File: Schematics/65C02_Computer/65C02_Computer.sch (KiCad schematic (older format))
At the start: 11 parts

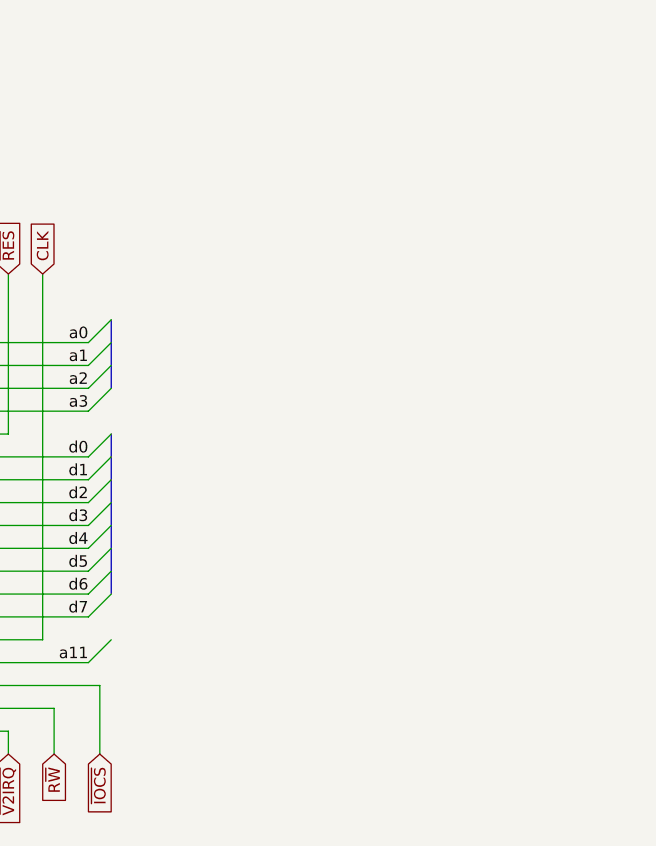
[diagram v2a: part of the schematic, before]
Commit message: Added ACIA chip
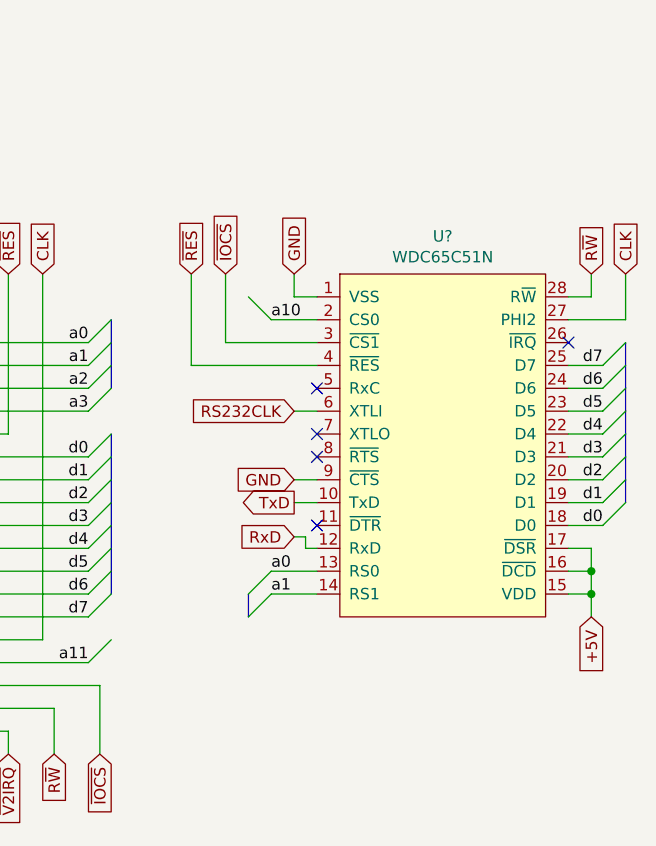
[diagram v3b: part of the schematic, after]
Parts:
- added U?: WDC65C51N, Package_DIP:DIP-28_W15.24mm_Socket, symbol 6502:WDC65C51N
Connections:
- net +5V: now also U?.15 (VDD), U?.16 (~DCD), U?.17 (~DSR)
- net CLK: now also U?.27 (PHI2)
- net GND: now also U?.1 (VSS), U?.9 (~CTS)
- net RS232CLK: now also U?.6 (XTLI)
- net R~W: now also U?.28 (R~W)
- net a0: now also U?.13 (RS0)
- net a1: now also U?.14 (RS1)
- net a10: now also U?.2 (CS0)
- net d0: now also U?.18 (D0)
- net d1: now also U?.19 (D1)
- net d2: now also U?.20 (D2)
- net d3: now also U?.21 (D3)
- net d4: now also U?.22 (D4)
- net d5: now also U?.23 (D5)
- net d6: now also U?.24 (D6)
- net d7: now also U?.25 (D7)
- net ~IOCS: now also U?.3 (~CS1)
- net ~RES: now also U?.4 (~RES)
- new net RxD: U?.12 (RxD)
- new net TxD: U?.10 (TxD)
- no-connect marks 15 -> 20
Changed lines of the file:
@@
 Wire Wire Line
 	5950 4600 5950 4500
+$Comp
+L 6502:WDC65C51N U?
+U 1 1 5E222305
+P 9100 3250
+F 0 "U?" H 9100 4165 50  0000 C CNN
+F 1 "WDC65C51N" H 9100 4074 50  0000 C CNN
+F 2 "Package_DIP:DIP-28_W15.24mm_Socket" H 9100 3250 50  0001 C CNN
+F 3 "https://www.westerndesigncenter.com/wdc/documentation/w65c51n.pdf" H 9100 3250 50  0001 C CNN
+	1    9100 3250
+	1    0    0    -1
+$EndComp
+Text GLabel 9750 4000 3    50   Input ~ 0
++5V
+Wire Wire Line
+	9650 3900 9750 3900
+Wire Wire Line
+	9750 3900 9750 4000
+Text GLabel 8450 2500 1    50   Input ~ 0
+GND
+Wire Wire Line
+	8450 2500 8450 2600
+Wire Wire Line
+	8450 2600 8550 2600
+NoConn ~ 8550 3200
+NoConn ~ 9650 2800
+NoConn ~ 8550 3300
+NoConn ~ 8550 3600
+NoConn ~ 8550 3000
+Wire Wire Line
+	9650 3800 9750 3800
+Wire Wire Line
+	9750 3800 9750 3900
+Connection ~ 9750 3900
+Wire Wire Line
+	9650 3700 9750 3700
+Wire Wire Line
+	9750 3700 9750 3800
+Connection ~ 9750 3800
+Text GLabel 9750 2500 1    50   Input ~ 0
+R~W
+Wire Wire Line
+	9750 2500 9750 2600
+Wire Wire Line
+	9750 2600 9650 2600
+Text GLabel 9900 2500 1    50   Input ~ 0
+CLK
+Wire Wire Line
+	9900 2500 9900 2700
+Wire Wire Line
+	9900 2700 9650 2700
+Text Label 9800 3600 2    50   ~ 0
+d0
+Text Label 9800 3500 2    50   ~ 0
+d1
+Text Label 9800 3400 2    50   ~ 0
+d2
+Text Label 9800 3300 2    50   ~ 0
+d3
+Text Label 9800 3200 2    50   ~ 0
+d4
+Text Label 9800 3100 2    50   ~ 0
+d5
+Text Label 9800 3000 2    50   ~ 0
+d6
+Text Label 9800 2900 2    50   ~ 0
+d7
+Wire Wire Line
+	9650 2900 9800 2900
+Wire Wire Line
+	9650 3000 9800 3000
+Wire Wire Line
+	9650 3100 9800 3100
+Wire Wire Line
+	9650 3200 9800 3200
+Wire Wire Line
+	9650 3300 9800 3300
+Wire Wire Line
+	9650 3400 9800 3400
+Wire Wire Line
+	9650 3500 9800 3500
+Wire Wire Line
+	9650 3600 9800 3600
+Entry Wire Line
+	9800 2900 9900 2800
+Entry Wire Line
+	9800 3000 9900 2900
+Entry Wire Line
+	9800 3100 9900 3000
+Entry Wire Line
+	9800 3200 9900 3100
+Entry Wire Line
+	9800 3300 9900 3200
+Entry Wire Line
+	9800 3400 9900 3300
+Entry Wire Line
+	9800 3500 9900 3400
+Entry Wire Line
+	9800 3600 9900 3500
+Text Label 8350 2700 0    50   ~ 0
+a10
+Text GLabel 8150 2500 1    50   Input ~ 0
+~IOCS
+Wire Wire Line
+	8150 2500 8150 2800
+Wire Wire Line
+	8150 2800 8550 2800
+Wire Wire Line
+	8550 2700 8350 2700
+Entry Wire Line
+	8250 2600 8350 2700
+Text GLabel 8000 2500 1    50   Input ~ 0
+~RES
+Wire Wire Line
+	8000 2500 8000 2900
+Wire Wire Line
+	8000 2900 8550 2900
+Text GLabel 8450 3100 0    50   Input ~ 0
+RS232CLK
+Wire Wire Line
+	8450 3100 8550 3100
+Text Label 8350 3800 0    50   ~ 0
+a0
+Text Label 8350 3900 0    50   ~ 0
+a1
+Wire Wire Line
+	8350 3900 8550 3900
+Wire Wire Line
+	8350 3800 8550 3800
+Entry Wire Line
+	8250 3900 8350 3800
+Entry Wire Line
+	8250 4000 8350 3900
+Wire Bus Line
+	8250 3900 8250 4000
+Text GLabel 8450 3400 0    50   Input ~ 0
+GND
+Wire Wire Line
+	8450 3400 8550 3400
+Text GLabel 8450 3500 0    50   Output ~ 0
+TxD
+Wire Wire Line
+	8550 3500 8450 3500
+Text GLabel 8450 3650 0    50   Input ~ 0
+RxD
+Wire Wire Line
+	8450 3650 8500 3650
+Wire Wire Line
+	8500 3650 8500 3700
+Wire Wire Line
+	8500 3700 8550 3700
 Wire Bus Line
 	3050 4200 3050 4500
@@
 	5650 3600 5650 4300
 Wire Bus Line
+	9900 2800 9900 3500
+Wire Bus Line
 	1400 3500 1400 4600

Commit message: Added RAM and ROM modules to schematic
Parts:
- added U? (x3): 74HC00, symbol 74xx:74HC00
- added U?: 74HC02, symbol 74xx:74HC02
- added U?: 62256, Package_DIP:DIP-28_W15.24mm_Socket, symbol 6502:62256
- added U?: 28C256, Package_DIP:DIP-28_W15.24mm_Socket, symbol 6502:28C256
- U?: value WDC65C02S -> 65C02S; footprint (none) -> Package_DIP:DIP-40_W15.24mm_Socket; symbol 6502:WDC65C02S -> 6502:65C02S
- U? (x2): value WDC65C22S -> 65C22S; symbol 6502:WDC65C22S -> 6502:65C22S
- U?: value WDC65C51N -> 65C51N; symbol 6502:WDC65C51N -> 6502:65C51N
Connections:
- net +5V: now also U?.27 (~WE), U?.28 (VCC), U?.28 (VCC)
- net CLK: now also U?.5
- net GND: now also U?.14 (GND), U?.14 (GND)
- net R~W: now also U?.27 (~WE)
- net a0: now also U?.10 (A0), U?.10 (A0)
- net a1: now also U?.9 (A1), U?.9 (A1)
- net a10: now also U?.21 (A10), U?.21 (A10)
- net a11: now also U?.23 (A11), U?.23 (A11)
- net a12: now also U?.2 (A12), U?.2 (A12)
- net a13: now also U?.10, U?.11, U?.26 (A13), U?.26 (A13)
- net a14: now also U?.1 (A14), U?.1 (A14), U?.12
- net a15: now also U?.1, U?.2
- net a2: now also U?.8 (A2), U?.8 (A2)
- net a3: now also U?.7 (A3), U?.7 (A3)
- net a4: now also U?.6 (A4), U?.6 (A4)
- net a5: now also U?.5 (A5), U?.5 (A5)
- net a6: now also U?.4 (A6), U?.4 (A6)
- net a7: now also U?.3 (A7), U?.3 (A7)
- net a8: now also U?.25 (A8), U?.25 (A8)
- net a9: now also U?.24 (A9), U?.24 (A9)
- net d0: now also U?.11 (D0), U?.11 (D0)
- net d1: now also U?.12 (D1), U?.12 (D1)
- net d2: now also U?.13 (D2), U?.13 (D2)
- net d3: now also U?.15 (D3), U?.15 (D3)
- net d4: now also U?.16 (D4), U?.16 (D4)
- net d5: now also U?.17 (D5), U?.17 (D5)
- net d6: now also U?.18 (D6), U?.18 (D6)
- net d7: now also U?.19 (D7), U?.19 (D7)
- net ~IOCS: now also U?.8
- new net ~RAM_CS: U?.20 (~CE), U?.22 (~OE), U?.6
- new net ~ROM_CS: U?.13, U?.20 (~CE), U?.9
- new net ~ROM_OE: U?.22 (~OE), U?.3, U?.4
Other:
- moved on the sheet: U?

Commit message: Added footprints to components
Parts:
- C? (x2): footprint (none) -> Capacitor_THT:C_Disc_D3.4mm_W2.1mm_P2.50mm
- R? (x3): footprint (none) -> Resistor_THT:R_Axial_DIN0207_L6.3mm_D2.5mm_P7.62mm_Horizontal
- SW?: footprint (none) -> Button_Switch_THT:SW_PUSH_6mm_H4.3mm
- U? (x2): footprint (none) -> Package_DIP:DIP-14_W7.62mm_Socket
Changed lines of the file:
@@
 F 0 "U?" H 6950 2125 50  0000 C CNN
 F 1 "74HC02" H 6950 2034 50  0000 C CNN
-F 2 "" H 6950 1800 50  0001 C CNN
+F 2 "Package_DIP:DIP-14_W7.62mm_Socket" H 6950 1800 50  0001 C CNN
 F 3 "http://www.ti.com/lit/gpn/sn74hc02" H 6950 1800 50  0001 C CNN
 	4    6950 1800
@@
 F 0 "U?" H 6950 1425 50  0000 C CNN
 F 1 "74HC00" H 6950 1334 50  0000 C CNN
-F 2 "" H 6950 1100 50  0001 C CNN
+F 2 "Package_DIP:DIP-14_W7.62mm_Socket" H 6950 1100 50  0001 C CNN
 F 3 "http://www.ti.com/lit/gpn/sn74hc00" H 6950 1100 50  0001 C CNN
 	1    6950 1100
@@
 F 0 "SW?" V 2650 1750 50  0000 R CNN
 F 1 "RESET" V 2550 1800 50  0000 R CNN
-F 2 "" H 2600 1650 50  0001 C CNN
+F 2 "Button_Switch_THT:SW_PUSH_6mm_H4.3mm" H 2600 1650 50  0001 C CNN
 F 3 "~" H 2600 1650 50  0001 C CNN
 	1    2600 1450
@@
 F 0 "C?" H 3015 1496 50  0000 L CNN
 F 1 "0.1uF" H 3015 1405 50  0000 L CNN
-F 2 "" H 2938 1300 50  0001 C CNN
+F 2 "Capacitor_THT:C_Disc_D3.4mm_W2.1mm_P2.50mm" H 2938 1300 50  0001 C CNN
 F 3 "~" H 2900 1450 50  0001 C CNN
 	1    2900 1450
@@
 F 0 "R?" V 2300 1150 50  0000 C CNN
 F 1 "1K" V 2400 1150 50  0000 C CNN
-F 2 "" V 2330 1150 50  0001 C CNN
+F 2 "Resistor_THT:R_Axial_DIN0207_L6.3mm_D2.5mm_P7.62mm_Horizontal" V 2330 1150 50  0001 C CNN
 F 3 "~" H 2400 1150 50  0001 C CNN
 	1    2400 1150
@@
 F 0 "C?" H 1415 1496 50  0000 L CNN
 F 1 "0.1uF" H 1415 1405 50  0000 L CNN
-F 2 "" H 1338 1300 50  0001 C CNN
+F 2 "Capacitor_THT:C_Disc_D3.4mm_W2.1mm_P2.50mm" H 1338 1300 50  0001 C CNN
 F 3 "~" H 1300 1450 50  0001 C CNN
 	1    1300 1450
@@
 $EndComp
 $Comp
-L power:GND #PWR?
+L power:GND #PWR0101
 U 1 1 5E15AF3A
 P 1300 1700
-F 0 "#PWR?" H 1300 1450 50  0001 C CNN
+F 0 "#PWR0101" H 1300 1450 50  0001 C CNN
 F 1 "GND" H 1305 1527 50  0000 C CNN
 F 2 "" H 1300 1700 50  0001 C CNN
@@
 $EndComp
 $Comp
-L power:+5V #PWR?
+L power:+5V #PWR0102
 U 1 1 5E15AAC6
 P 1300 1200
-F 0 "#PWR?" H 1300 1050 50  0001 C CNN
+F 0 "#PWR0102" H 1300 1050 50  0001 C CNN
 F 1 "+5V" H 1315 1373 50  0000 C CNN
 F 2 "" H 1300 1200 50  0001 C CNN
@@
 F 0 "R?" V 1300 3100 50  0000 C CNN
 F 1 "1K" V 1400 3100 50  0000 C CNN
-F 2 "" V 1330 3100 50  0001 C CNN
+F 2 "Resistor_THT:R_Axial_DIN0207_L6.3mm_D2.5mm_P7.62mm_Horizontal" V 1330 3100 50  0001 C CNN
 F 3 "~" H 1400 3100 50  0001 C CNN
 	1    1400 3100
@@
 F 0 "R?" V 1300 2700 50  0000 C CNN
 F 1 "1K" V 1400 2700 50  0000 C CNN
-F 2 "" V 1330 2700 50  0001 C CNN
+F 2 "Resistor_THT:R_Axial_DIN0207_L6.3mm_D2.5mm_P7.62mm_Horizontal" V 1330 2700 50  0001 C CNN
 F 3 "~" H 1400 2700 50  0001 C CNN
 	1    1400 2700

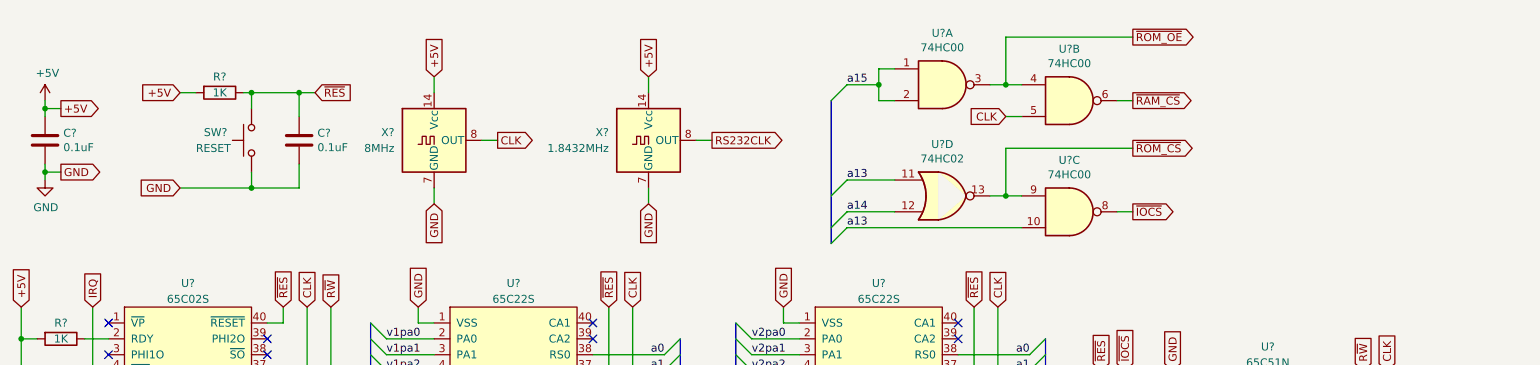
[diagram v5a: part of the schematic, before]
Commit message: Added automatic RESET on power-on
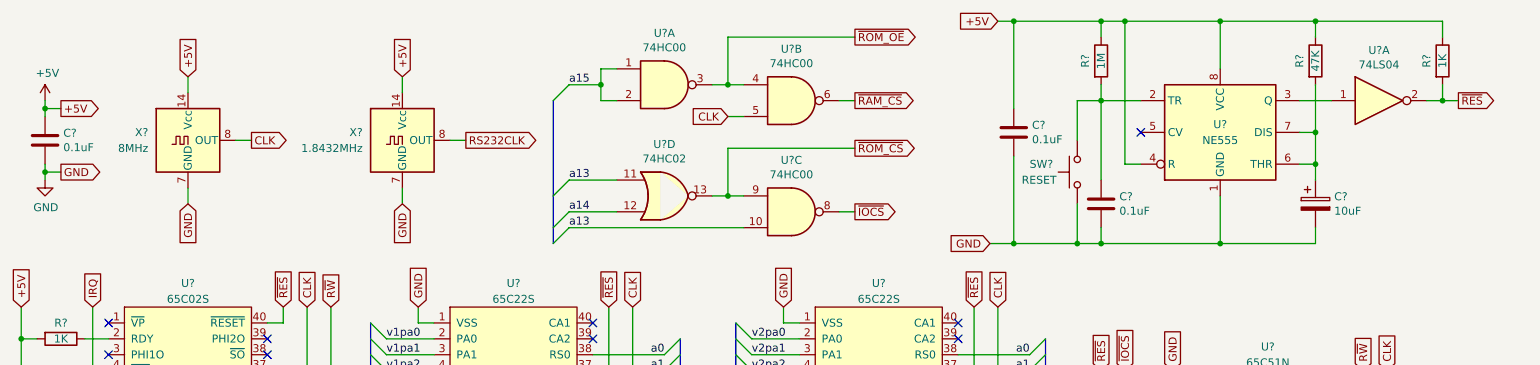
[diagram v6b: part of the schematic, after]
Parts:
- removed C?: 0.1uF, Capacitor_THT:C_Disc_D3.4mm_W2.1mm_P2.50mm, symbol Device:C
- removed R?: 1K, Resistor_THT:R_Axial_DIN0207_L6.3mm_D2.5mm_P7.62mm_Horizontal, symbol Device:R
- removed SW?: RESET, Button_Switch_THT:SW_PUSH_6mm_H4.3mm, symbol Switch:SW_Push
- added C?: 10uF, Capacitor_THT:CP_Radial_D5.0mm_P2.50mm, symbol Device:CP
- added C? (x2): 0.1uF, Capacitor_THT:C_Disc_D3.4mm_W2.1mm_P2.50mm, symbol Device:C
- added R?: 47K, Resistor_THT:R_Axial_DIN0207_L6.3mm_D2.5mm_P7.62mm_Horizontal, symbol Device:R
- added R?: 1M, Resistor_THT:R_Axial_DIN0207_L6.3mm_D2.5mm_P7.62mm_Horizontal, symbol Device:R
- added R?: 1K, Resistor_THT:R_Axial_DIN0207_L6.3mm_D2.5mm_P7.62mm_Horizontal, symbol Device:R
- added SW?: RESET, Button_Switch_THT:SW_PUSH_6mm_H4.3mm, symbol Switch:SW_Push
- added U?: NE555, Package_DIP:DIP-8_W7.62mm_Socket, symbol Timer:NE555
- added U?: 74LS04, Package_DIP:DIP-14_W7.62mm_Socket, symbol 74xx:74LS04
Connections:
- net +5V: now also C?.1, R?.1, R?.1, R?.1, U?.4 (R), U?.8 (VCC)
- net GND: now also C?.2, C?.2, C?.2, SW?.1, U?.1 (GND)
- net ~RES: now also R?.2, U?.2
- new net: C?.1, R?.2, SW?.2, U?.2 (TR)
- new net: U?.1, U?.3 (Q)
- new net: C?.1, R?.2, U?.6 (THR), U?.7 (DIS)
- no-connect marks 20 -> 21
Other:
- moved on the sheet: U?A, U?B, U?C, U?D, X?

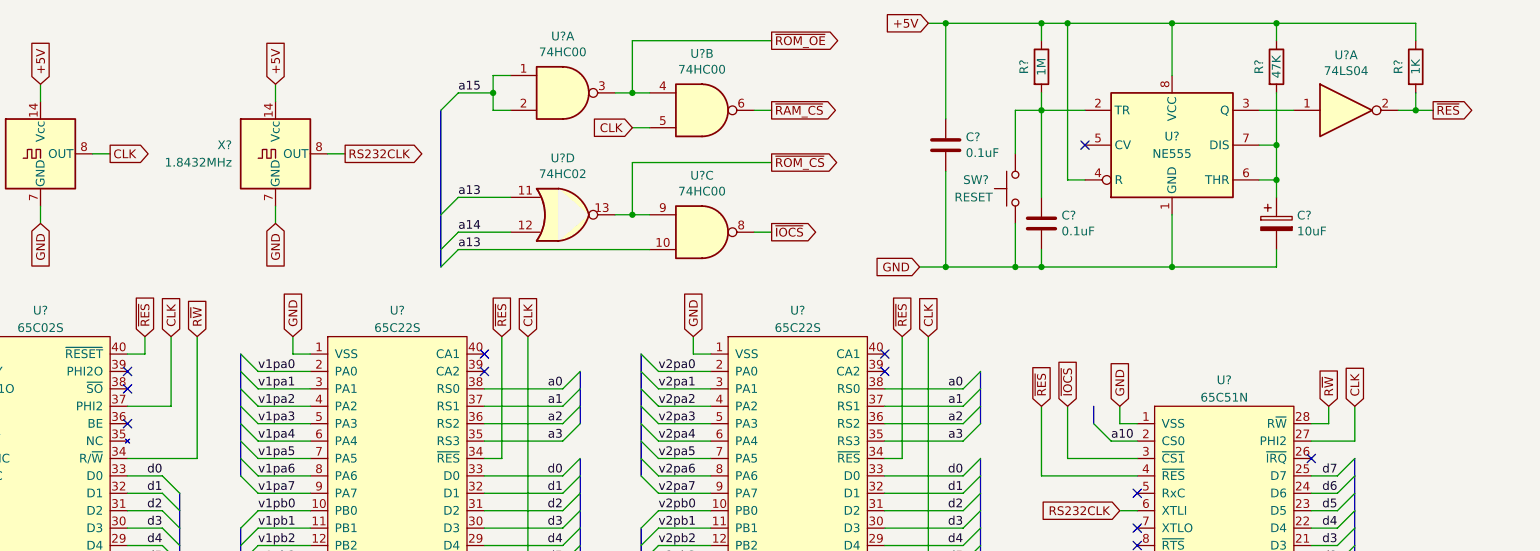
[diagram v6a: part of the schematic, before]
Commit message: Fixed issue with Bus Enable connection, replaced inverter by NAND
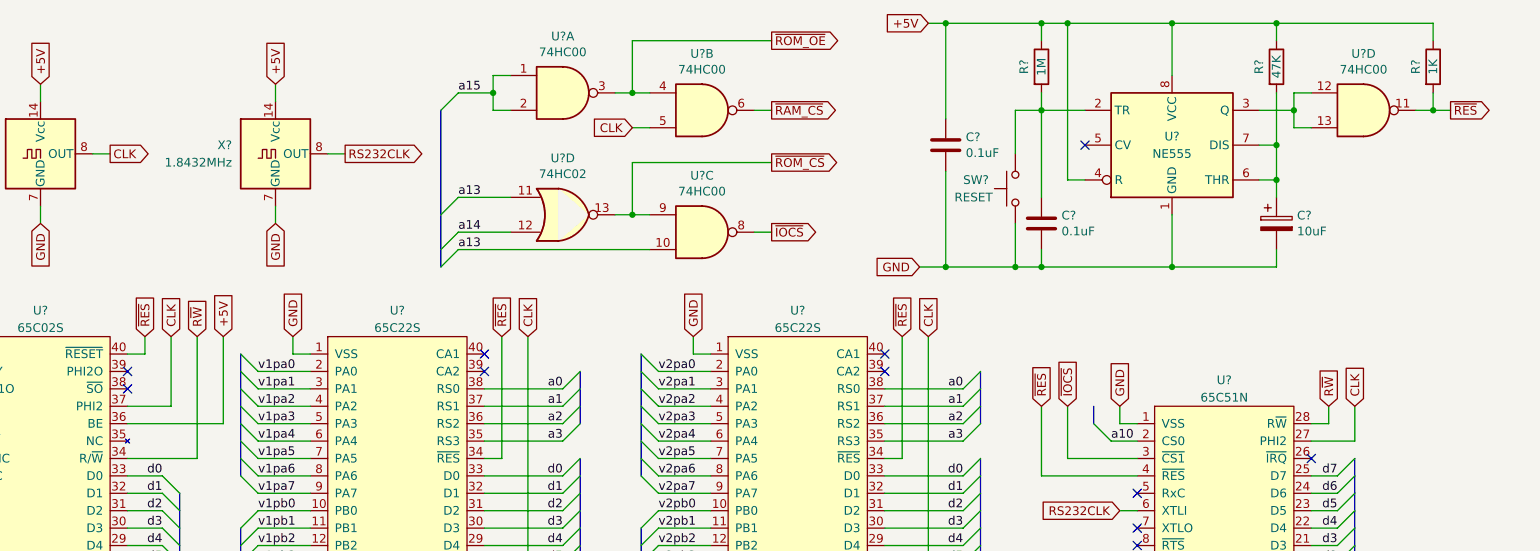
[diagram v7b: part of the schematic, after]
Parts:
- removed U?: 74LS04, Package_DIP:DIP-14_W7.62mm_Socket, symbol 74xx:74LS04
- added U?: 74HC00, symbol 74xx:74HC00
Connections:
- net +5V: now also U?.36 (BE)
- net ~RES: now also U?.11
- net at U?.3 (Q): now also U?.12, U?.13
- no-connect marks 21 -> 20
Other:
- moved on the sheet: R?
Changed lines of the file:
@@
 Wire Wire Line
 	3100 3200 2700 3200
-NoConn ~ 2700 3000
 NoConn ~ 2700 2800
 NoConn ~ 2700 2700
@@
 Wire Wire Line
 	7950 700  8100 700
-$Comp
-L 74xx:74LS04 U?
-U 1 1 5E4F36D6
-P 9700 1200
-F 0 "U?" H 9700 1517 50  0000 C CNN
-F 1 "74LS04" H 9700 1426 50  0000 C CNN
-F 2 "Package_DIP:DIP-14_W7.62mm_Socket" H 9700 1200 50  0001 C CNN
-F 3 "http://www.ti.com/lit/gpn/sn74LS04" H 9700 1200 50  0001 C CNN
-	1    9700 1200
-	1    0    0    -1
-$EndComp
 Wire Wire Line
 	9200 1200 9400 1200
-Text GLabel 10200 1200 2    50   Output ~ 0
+Text GLabel 10300 1200 2    50   Output ~ 0
 ~RES
 Wire Wire Line
-	10000 1200 10100 1200
+	10100 1200 10200 1200
 $Comp
 L Device:R R?
 U 1 1 5E552FBE
-P 10100 950
-F 0 "R?" V 10000 950 50  0000 C CNN
-F 1 "1K" V 10100 950 50  0000 C CNN
-F 2 "Resistor_THT:R_Axial_DIN0207_L6.3mm_D2.5mm_P7.62mm_Horizontal" V 10030 950 50  0001 C CNN
-F 3 "~" H 10100 950 50  0001 C CNN
-	1    10100 950
+P 10200 950
+F 0 "R?" V 10100 950 50  0000 C CNN
+F 1 "1K" V 10200 950 50  0000 C CNN
+F 2 "Resistor_THT:R_Axial_DIN0207_L6.3mm_D2.5mm_P7.62mm_Horizontal" V 10130 950 50  0001 C CNN
+F 3 "~" H 10200 950 50  0001 C CNN
+	1    10200 950
 	1    0    0    -1
 $EndComp
@@
 Connection ~ 8700 700
 Wire Wire Line
-	10100 800  10100 700
-Wire Wire Line
-	10100 700  9300 700
+	10200 800  10200 700
+Wire Wire Line
+	10200 700  9300 700
 Connection ~ 9300 700
 Wire Wire Line
-	10100 1100 10100 1200
-Connection ~ 10100 1200
-Wire Wire Line
-	10100 1200 10200 1200
+	10200 1100 10200 1200
+Connection ~ 10200 1200
+Wire Wire Line
+	10200 1200 10300 1200
 Wire Wire Line
 	8700 1000 8700 700
@@
 Wire Wire Line
 	7400 1250 7400 700
+Connection ~ 7400 700
+Wire Wire Line
+	7400 700  7950 700
+Text GLabel 3250 2500 1    50   Input ~ 0
++5V
+Wire Wire Line
+	2700 3000 3250 3000
+Wire Wire Line
+	3250 3000 3250 2500
+$Comp
+L 74xx:74HC00 U?
+U 4 1 5E218D59
+P 9800 1200
+F 0 "U?" H 9800 1525 50  0000 C CNN
+F 1 "74HC00" H 9800 1434 50  0000 C CNN
+F 2 "" H 9800 1200 50  0001 C CNN
+F 3 "http://www.ti.com/lit/gpn/sn74hc00" H 9800 1200 50  0001 C CNN
+	4    9800 1200
+	1    0    0    -1
+$EndComp
+Wire Wire Line
+	9500 1100 9400 1100
+Wire Wire Line
+	9400 1100 9400 1200
+Wire Wire Line
+	9400 1300 9500 1300
+Connection ~ 9400 1200
+Wire Wire Line
+	9400 1200 9400 1300
 Wire Bus Line
 	3500 6750 3500 6950
@@
 Wire Bus Line
 	1400 3500 1400 4600
-Connection ~ 7400 700
-Wire Wire Line
-	7400 700  7950 700
 $EndSCHEMATC

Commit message: Small changes to glue logic
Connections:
- net a13: now also U?.6; no longer U?.11
- net a14: now also U?.5; no longer U?.12
- net ~ROM_CS: now also U?.4; no longer U?.13
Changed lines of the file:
@@
 	4800 1100 4800 1000
 Text Label 4600 1700 0    50   ~ 0
+a14
+Text Label 4600 1900 0    50   ~ 0
 a13
-Text Label 4600 1900 0    50   ~ 0
-a14
-Text Label 4600 2000 0    50   ~ 0
-a13
-Wire Wire Line
-	5700 2000 4600 2000
-Wire Wire Line
-	4900 1900 4600 1900
+Wire Wire Line
+	4900 1900 4800 1900
 Wire Wire Line
 	4900 1700 4600 1700
@@
 	4500 2000 4600 1900
 Entry Wire Line
-	4500 2100 4600 2000
-Entry Wire Line
 	4500 1200 4600 1100
 Text GLabel 6400 1900 2    50   Output ~ 0
@@
 $Comp
 L 74xx:74HC02 U?
-U 4 1 5E1744DD
+U 2 1 5E1744DD
 P 5200 1800
 F 0 "U?" H 5200 2125 50  0000 C CNN
@@
 F 2 "Package_DIP:DIP-14_W7.62mm_Socket" H 5200 1800 50  0001 C CNN
 F 3 "http://www.ti.com/lit/gpn/sn74hc02" H 5200 1800 50  0001 C CNN
-	4    5200 1800
+	2    5200 1800
 	1    0    0    -1
 $EndComp
@@
 Wire Wire Line
 	9400 1200 9400 1300
+Wire Wire Line
+	4800 1900 4800 2000
+Wire Wire Line
+	4800 2000 5700 2000
 Wire Bus Line
 	3500 6750 3500 6950
@@
 	1450 6750 1450 6950
 Wire Bus Line
+	4500 1200 4500 2000
+Wire Bus Line
 	3000 4200 3000 4500
 Wire Bus Line
@@
 	7600 2700 7600 3000
 Wire Bus Line
-	4500 1200 4500 2100
-Wire Bus Line
 	5400 5950 5400 6450
 Wire Bus Line
@@
 Wire Bus Line
 	1400 3500 1400 4600
+Connection ~ 4800 1900
+Wire Wire Line
+	4800 1900 4600 1900
 $EndSCHEMATC
